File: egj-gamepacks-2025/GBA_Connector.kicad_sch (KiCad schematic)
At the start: 6 parts, among them J5 GameBoy_GamePak_AGB-002, U10 SP3012-06UTG, U6 SP3012-06UTG, U7 SP3012-06UTG, U8 SP3012-06UTG, U9 SP3012-06UTG

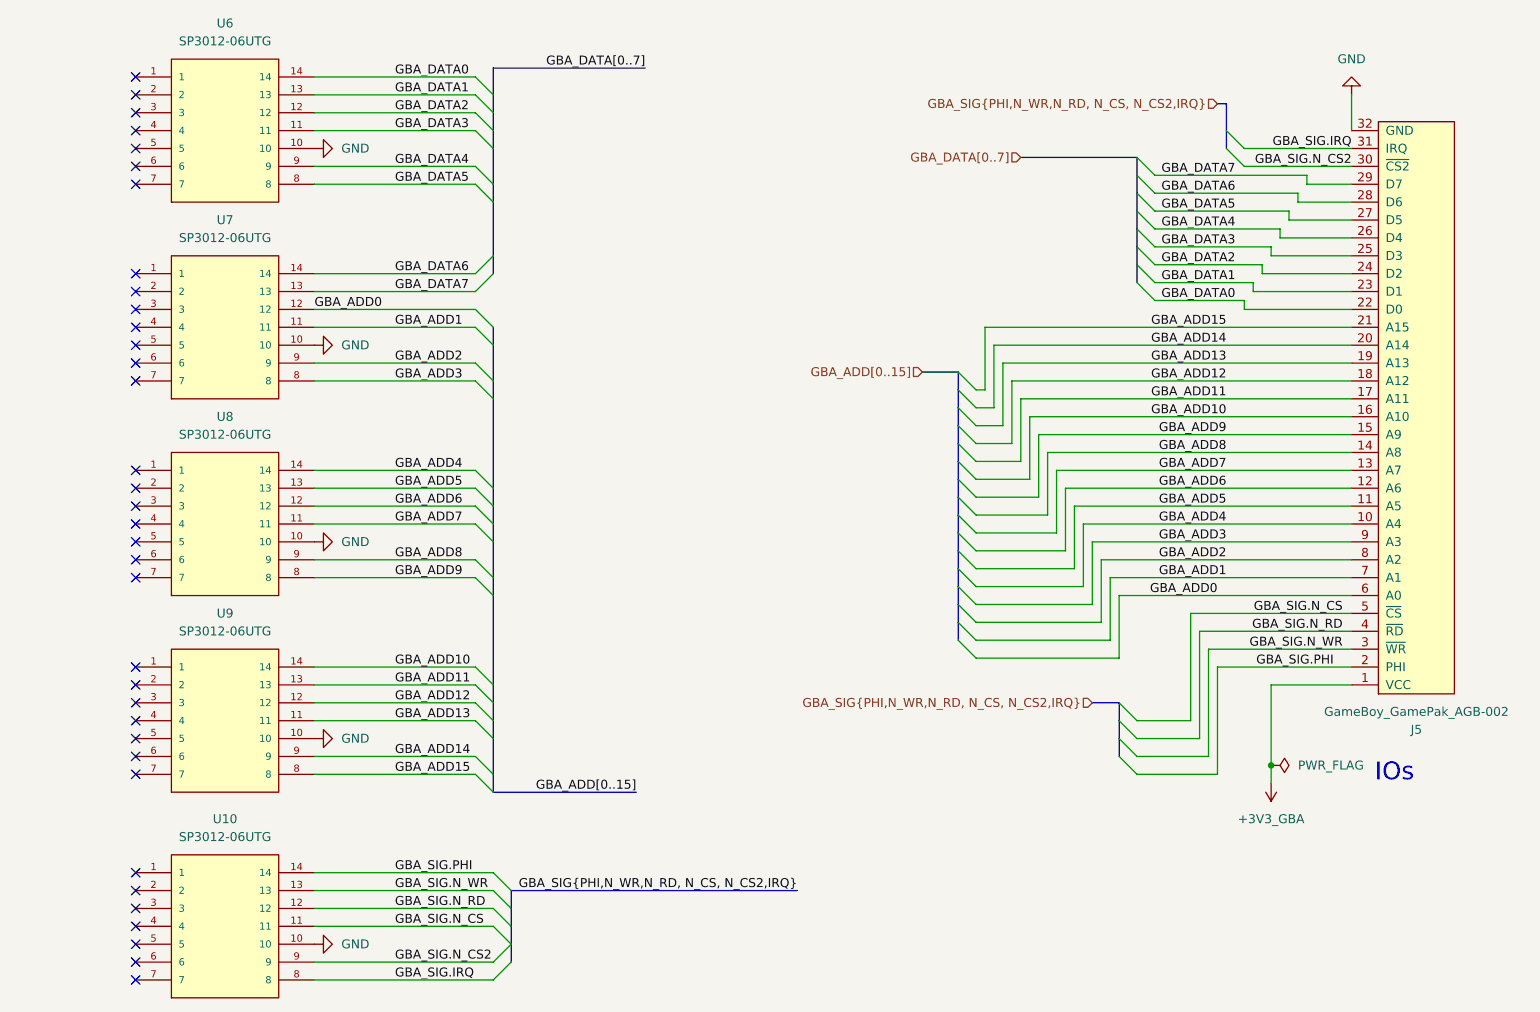
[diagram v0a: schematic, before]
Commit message: FIX: schematic fixes, JLCPCB parts with LCSC numbers and GBA bus GPIO remap
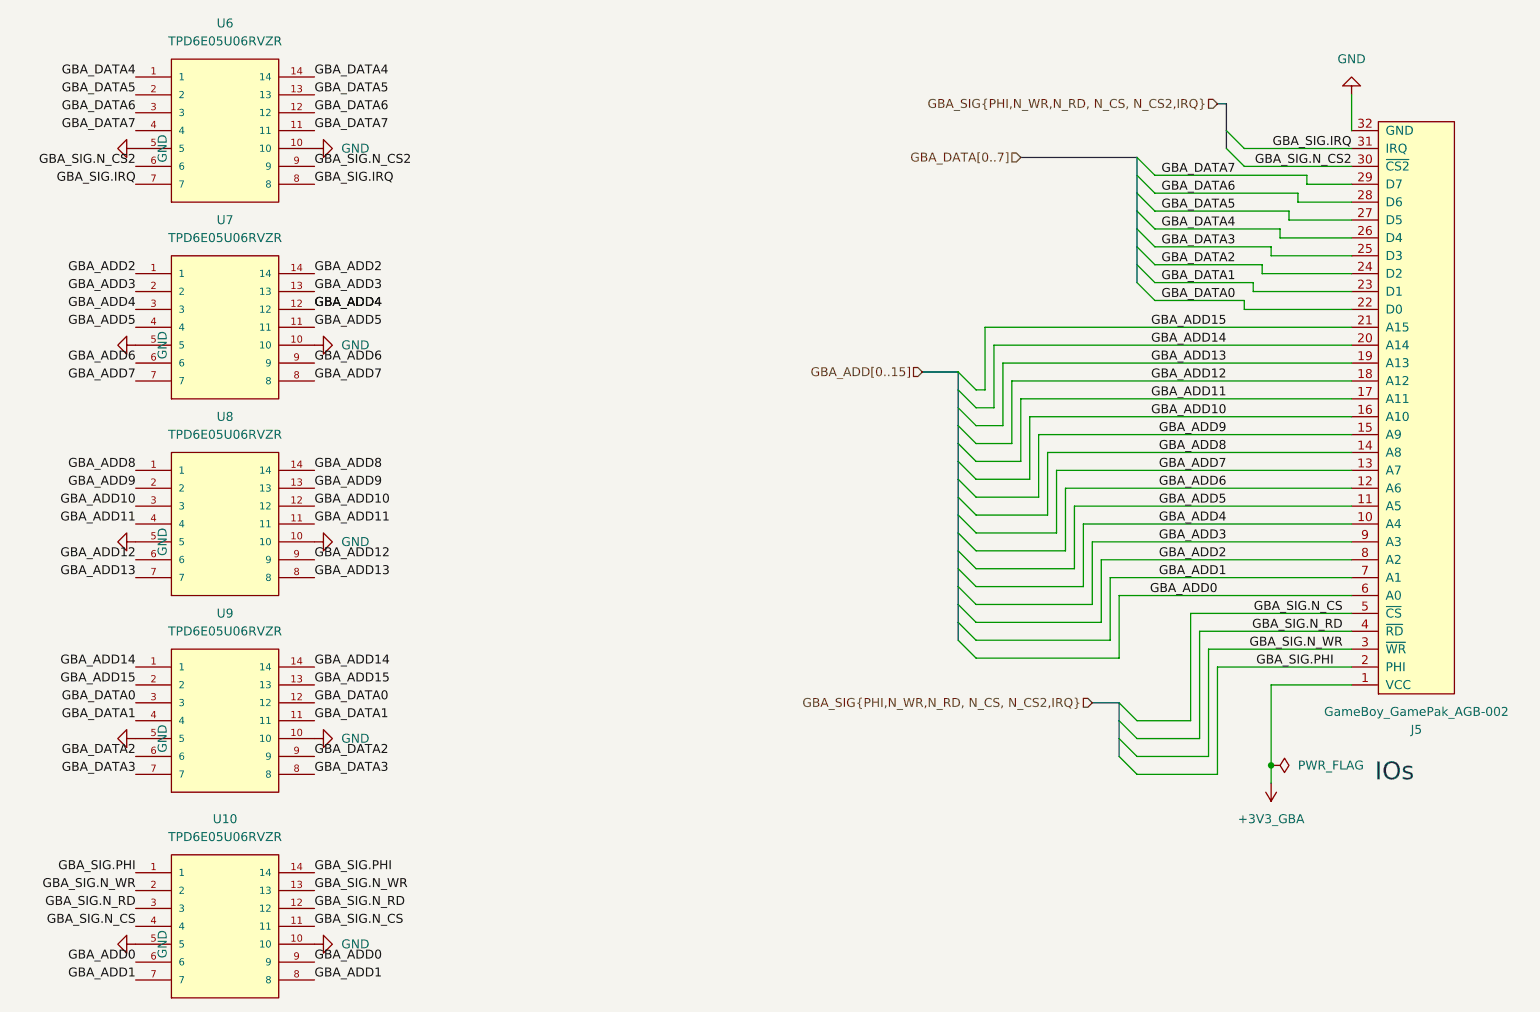
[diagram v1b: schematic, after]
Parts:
- U10, U6, U7, U8, U9: value SP3012-06UTG -> TPD6E05U06RVZR; LCSC (none) -> C962978
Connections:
- net GBA_ADD0: now also U10.6, U10.9; no longer U7.12
- net GBA_ADD1: now also U10.7, U10.8; no longer U7.11
- net GBA_ADD10: now also U8.12, U8.3; no longer U9.14
- net GBA_ADD11: now also U8.11, U8.4; no longer U9.13
- net GBA_ADD12: now also U8.6, U8.9; no longer U9.12
- net GBA_ADD13: now also U8.7, U8.8; no longer U9.11
- net GBA_ADD14: now also U9.1, U9.14; no longer U9.9
- net GBA_ADD15: now also U9.13, U9.2; no longer U9.8
- net GBA_ADD2: now also U7.1, U7.14; no longer U7.9
- net GBA_ADD3: now also U7.13, U7.2; no longer U7.8
- net GBA_ADD4: now also U7.12, U7.3; no longer U8.14
- net GBA_ADD5: now also U7.11, U7.4; no longer U8.13
- net GBA_ADD6: now also U7.6, U7.9; no longer U8.12
- net GBA_ADD7: now also U7.7, U7.8; no longer U8.11
- net GBA_ADD8: now also U8.1, U8.14; no longer U8.9
- net GBA_ADD9: now also U8.13, U8.2; no longer U8.8
- net GBA_DATA0: now also U9.12, U9.3; no longer U6.14
- net GBA_DATA1: now also U9.11, U9.4; no longer U6.13
- net GBA_DATA2: now also U9.6, U9.9; no longer U6.12
- net GBA_DATA3: now also U9.7, U9.8; no longer U6.11
- net GBA_DATA4: now also U6.1, U6.14; no longer U6.9
- net GBA_DATA5: now also U6.13, U6.2; no longer U6.8
- net GBA_DATA6: now also U6.12, U6.3; no longer U7.14
- net GBA_DATA7: now also U6.11, U6.4; no longer U7.13
- net GBA_SIG.IRQ: now also U6.7, U6.8; no longer U10.8
- net GBA_SIG.N_CS: now also U10.4
- net GBA_SIG.N_CS2: now also U6.6, U6.9; no longer U10.9
- net GBA_SIG.N_RD: now also U10.3
- net GBA_SIG.N_WR: now also U10.2
- net GBA_SIG.PHI: now also U10.1
- net GND: now also U10.5, U6.5, U7.5, U8.5, U9.5
- no-connect marks 35 -> 0

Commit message: FIX: RP2350 regulator inductor, I2C pull-ups, DVDD decoupling and drop second flash option
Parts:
- J5: now left out of the parts list
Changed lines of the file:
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@@
 		(unit 1)
 		(exclude_from_sim no)
-		(in_bom yes)
+		(in_bom no)
 		(on_board yes)
 		(dnp no)
